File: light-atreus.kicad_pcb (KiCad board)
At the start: 2 copper layers, 37.4 x 44.1 mm, 8 parts, among them J1 USB_OTG, J2 CONN_01X02, J3 CONN_01X02, J4 USB_OTG, J5 CONN_01X02, J6 CONN_01X02

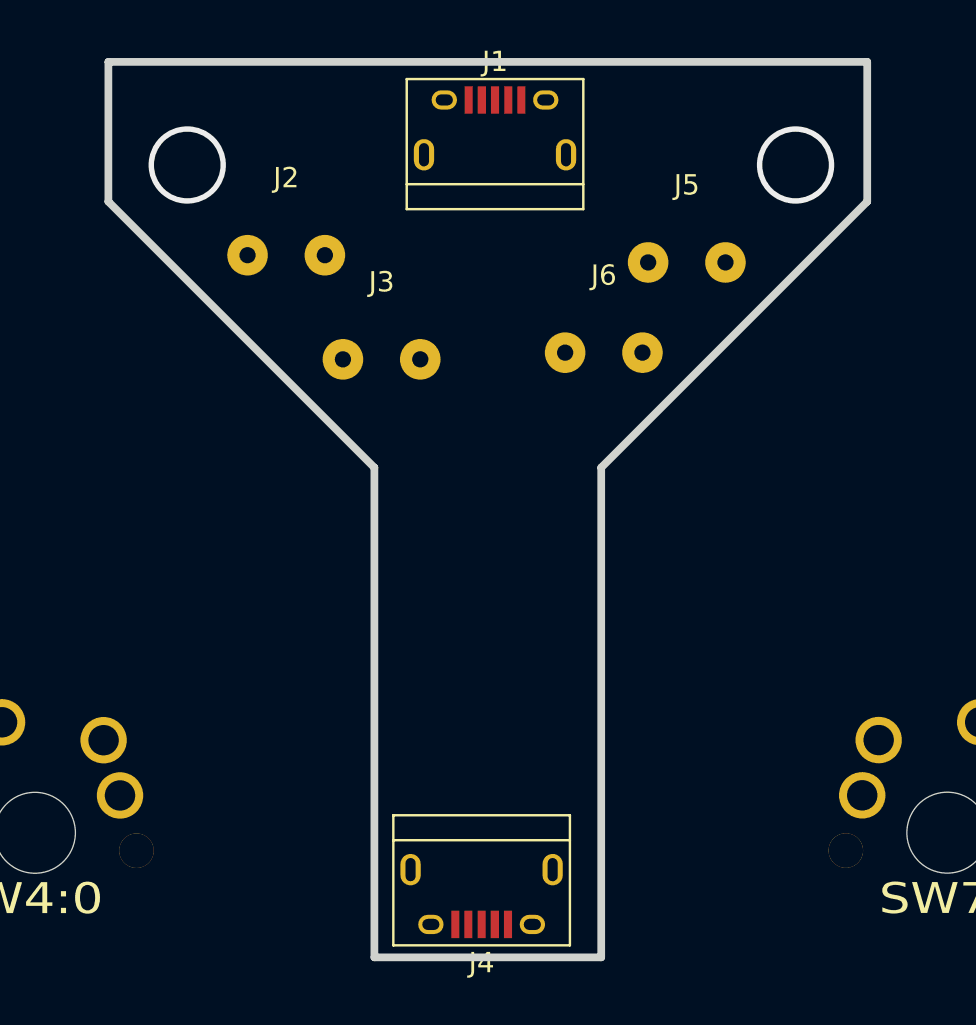
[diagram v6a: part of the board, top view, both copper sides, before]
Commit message: Add backside ground pour
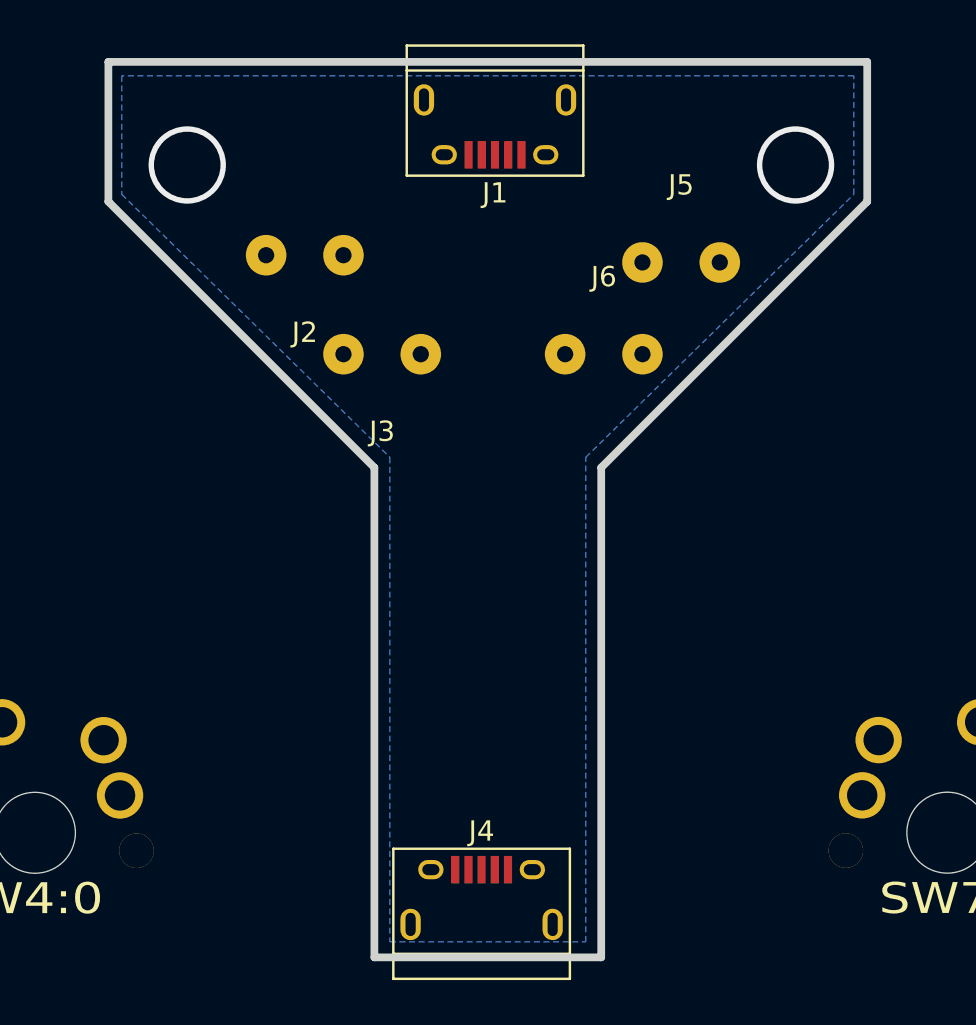
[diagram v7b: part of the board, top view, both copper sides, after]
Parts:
- moved J2 0.91 mm to (123.6, 99.3), turned to 180 degrees
- moved J5 0.28 mm to (142.1, 99.6)
- moved J3 0.26 mm to (127.4, 104.1), turned to 180 degrees
- moved J6 0.08 mm to (138.3, 104.1)
- turned J1 to 180 degrees
- turned J4 to 0 degrees
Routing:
- added copper zone on B.Cu, net /GND
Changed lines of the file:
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@@
   )
   (module Connectors:USB_Micro-B (layer Front)
-    (at 132.9436 92.964)
+    (at 132.9436 92.964 180)
     (descr "Micro USB Type B Receptacle")
     (tags "USB USB_B USB_micro USB_OTG")
     (attr smd)
-    (fp_text reference J1 (at 0 -3.24) (layer F.SilkS)
+    (fp_text reference J1 (at 0 -3.24 180) (layer F.SilkS)
       (effects (font (size 1 1) (thickness 0.15)))
     )
-    (fp_text value USB_OTG (at 0 5.01) (layer F.Fab)
+    (fp_text value USB_OTG (at 0 5.01 180) (layer F.Fab)
       (effects (font (size 1 1) (thickness 0.15)))
     )
@@
     (fp_line (start 4.6 -2.59) (end 4.6 4.26) (layer F.CrtYd) (width 0.05))
     (fp_line (start -4.6 -2.59) (end 4.6 -2.59) (layer F.CrtYd) (width 0.05))
-    (pad 6 thru_hole oval (at 3.5 1.35 90) (size 1.55 1) (drill oval 1.15 0.5) (layers *.Cu *.Mask)
+    (pad 6 thru_hole oval (at 3.5 1.35 270) (size 1.55 1) (drill oval 1.15 0.5) (layers *.Cu *.Mask)
       (net 5 "Net-(J1-Pad6)"))
-    (pad 6 thru_hole oval (at -3.5 1.35 90) (size 1.55 1) (drill oval 1.15 0.5) (layers *.Cu *.Mask)
+    (pad 6 thru_hole oval (at -3.5 1.35 270) (size 1.55 1) (drill oval 1.15 0.5) (layers *.Cu *.Mask)
       (net 5 "Net-(J1-Pad6)"))
-    (pad 6 thru_hole oval (at 2.5 -1.35 90) (size 0.95 1.25) (drill oval 0.55 0.85) (layers *.Cu *.Mask)
+    (pad 6 thru_hole oval (at 2.5 -1.35 270) (size 0.95 1.25) (drill oval 0.55 0.85) (layers *.Cu *.Mask)
       (net 5 "Net-(J1-Pad6)"))
-    (pad 6 thru_hole oval (at -2.5 -1.35 90) (size 0.95 1.25) (drill oval 0.55 0.85) (layers *.Cu *.Mask)
+    (pad 6 thru_hole oval (at -2.5 -1.35 270) (size 0.95 1.25) (drill oval 0.55 0.85) (layers *.Cu *.Mask)
       (net 5 "Net-(J1-Pad6)"))
-    (pad 5 smd rect (at 1.3 -1.35 90) (size 1.35 0.4) (layers Front F.Paste F.Mask)
+    (pad 5 smd rect (at 1.3 -1.35 270) (size 1.35 0.4) (layers Front F.Paste F.Mask)
       (net 9 /GND))
-    (pad 4 smd rect (at 0.65 -1.35 90) (size 1.35 0.4) (layers Front F.Paste F.Mask)
+    (pad 4 smd rect (at 0.65 -1.35 270) (size 1.35 0.4) (layers Front F.Paste F.Mask)
       (net 6 "Net-(J1-Pad4)"))
-    (pad 3 smd rect (at 0 -1.35 90) (size 1.35 0.4) (layers Front F.Paste F.Mask)
+    (pad 3 smd rect (at 0 -1.35 270) (size 1.35 0.4) (layers Front F.Paste F.Mask)
       (net 7 "Net-(J1-Pad3)"))
-    (pad 2 smd rect (at -0.65 -1.35 90) (size 1.35 0.4) (layers Front F.Paste F.Mask)
+    (pad 2 smd rect (at -0.65 -1.35 270) (size 1.35 0.4) (layers Front F.Paste F.Mask)
       (net 8 "Net-(J1-Pad2)"))
-    (pad 1 smd rect (at -1.3 -1.35 90) (size 1.35 0.4) (layers Front F.Paste F.Mask)
+    (pad 1 smd rect (at -1.3 -1.35 270) (size 1.35 0.4) (layers Front F.Paste F.Mask)
       (net 10 /VBUS))
   )
   (module Connectors:USB_Micro-B (layer Front)
-    (at 132.2832 130.8862 180)
+    (at 132.2832 130.8862)
     (descr "Micro USB Type B Receptacle")
     (tags "USB USB_B USB_micro USB_OTG")
     (attr smd)
-    (fp_text reference J4 (at 0 -3.24 180) (layer F.SilkS)
+    (fp_text reference J4 (at 0 -3.24) (layer F.SilkS)
       (effects (font (size 1 1) (thickness 0.15)))
     )
-    (fp_text value USB_OTG (at 0 5.01 180) (layer F.Fab)
+    (fp_text value USB_OTG (at 0 5.01) (layer F.Fab)
       (effects (font (size 1 1) (thickness 0.15)))
     )
@@
     (fp_line (start 4.35 2.8) (end -4.35 2.8) (layer F.SilkS) (width 0.12))
     (fp_line (start -4.35 4.03) (end -4.35 -2.38) (layer F.SilkS) (width 0.12))
-    (pad 1 smd rect (at -1.3 -1.35 270) (size 1.35 0.4) (layers Front F.Paste F.Mask)
+    (pad 1 smd rect (at -1.3 -1.35 90) (size 1.35 0.4) (layers Front F.Paste F.Mask)
       (net 10 /VBUS))
-    (pad 2 smd rect (at -0.65 -1.35 270) (size 1.35 0.4) (layers Front F.Paste F.Mask)
+    (pad 2 smd rect (at -0.65 -1.35 90) (size 1.35 0.4) (layers Front F.Paste F.Mask)
       (net 8 "Net-(J1-Pad2)"))
-    (pad 3 smd rect (at 0 -1.35 270) (size 1.35 0.4) (layers Front F.Paste F.Mask)
+    (pad 3 smd rect (at 0 -1.35 90) (size 1.35 0.4) (layers Front F.Paste F.Mask)
       (net 7 "Net-(J1-Pad3)"))
-    (pad 4 smd rect (at 0.65 -1.35 270) (size 1.35 0.4) (layers Front F.Paste F.Mask)
+    (pad 4 smd rect (at 0.65 -1.35 90) (size 1.35 0.4) (layers Front F.Paste F.Mask)
       (net 6 "Net-(J1-Pad4)"))
-    (pad 5 smd rect (at 1.3 -1.35 270) (size 1.35 0.4) (layers Front F.Paste F.Mask)
+    (pad 5 smd rect (at 1.3 -1.35 90) (size 1.35 0.4) (layers Front F.Paste F.Mask)
       (net 9 /GND))
-    (pad 6 thru_hole oval (at -2.5 -1.35 270) (size 0.95 1.25) (drill oval 0.55 0.85) (layers *.Cu *.Mask)
+    (pad 6 thru_hole oval (at -2.5 -1.35 90) (size 0.95 1.25) (drill oval 0.55 0.85) (layers *.Cu *.Mask)
       (net 5 "Net-(J1-Pad6)"))
-    (pad 6 thru_hole oval (at 2.5 -1.35 270) (size 0.95 1.25) (drill oval 0.55 0.85) (layers *.Cu *.Mask)
+    (pad 6 thru_hole oval (at 2.5 -1.35 90) (size 0.95 1.25) (drill oval 0.55 0.85) (layers *.Cu *.Mask)
       (net 5 "Net-(J1-Pad6)"))
-    (pad 6 thru_hole oval (at -3.5 1.35 270) (size 1.55 1) (drill oval 1.15 0.5) (layers *.Cu *.Mask)
+    (pad 6 thru_hole oval (at -3.5 1.35 90) (size 1.55 1) (drill oval 1.15 0.5) (layers *.Cu *.Mask)
       (net 5 "Net-(J1-Pad6)"))
-    (pad 6 thru_hole oval (at 3.5 1.35 270) (size 1.55 1) (drill oval 1.15 0.5) (layers *.Cu *.Mask)
+    (pad 6 thru_hole oval (at 3.5 1.35 90) (size 1.55 1) (drill oval 1.15 0.5) (layers *.Cu *.Mask)
       (net 5 "Net-(J1-Pad6)"))
   )
   (module custom_footprints:SolderWirePad_1x2-8mm (layer Front)
-    (at 122.6566 99.2632)
-    (fp_text reference J2 (at 0 -3.81) (layer F.SilkS)
+    (at 123.571 99.2632 180)
+    (fp_text reference J2 (at 0 -3.81 180) (layer F.SilkS)
       (effects (font (size 1 1) (thickness 0.15)))
     )
-    (fp_text value CONN_01X02 (at 0.635 2.54) (layer F.Fab)
+    (fp_text value CONN_01X02 (at 0.635 2.54 180) (layer F.Fab)
       (effects (font (size 1 1) (thickness 0.15)))
     )
-    (pad 2 thru_hole circle (at 1.905 0) (size 1.99898 1.99898) (drill 0.8001) (layers *.Cu *.Mask))
-    (pad 1 thru_hole circle (at -1.905 0) (size 1.99898 1.99898) (drill 0.8001) (layers *.Cu *.Mask)
+    (pad 2 thru_hole circle (at 1.905 0 180) (size 1.99898 1.99898) (drill 0.8001) (layers *.Cu *.Mask))
+    (pad 1 thru_hole circle (at -1.905 0 180) (size 1.99898 1.99898) (drill 0.8001) (layers *.Cu *.Mask)
       (net 10 /VBUS))
   )
   (module custom_footprints:SolderWirePad_1x2-8mm (layer Front)
-    (at 127.3556 104.394)
-    (fp_text reference J3 (at 0 -3.81) (layer F.SilkS)
+    (at 127.381 104.14 180)
+    (fp_text reference J3 (at 0 -3.81 180) (layer F.SilkS)
       (effects (font (size 1 1) (thickness 0.15)))
     )
-    (fp_text value CONN_01X02 (at 0.635 2.54) (layer F.Fab)
+    (fp_text value CONN_01X02 (at 0.635 2.54 180) (layer F.Fab)
       (effects (font (size 1 1) (thickness 0.15)))
     )
-    (pad 1 thru_hole circle (at -1.905 0) (size 1.99898 1.99898) (drill 0.8001) (layers *.Cu *.Mask)
+    (pad 1 thru_hole circle (at -1.905 0 180) (size 1.99898 1.99898) (drill 0.8001) (layers *.Cu *.Mask)
       (net 9 /GND))
-    (pad 2 thru_hole circle (at 1.905 0) (size 1.99898 1.99898) (drill 0.8001) (layers *.Cu *.Mask))
+    (pad 2 thru_hole circle (at 1.905 0 180) (size 1.99898 1.99898) (drill 0.8001) (layers *.Cu *.Mask))
   )
   (module custom_footprints:SolderWirePad_1x2-8mm (layer Front)
-    (at 142.3924 99.6188)
+    (at 142.113 99.6188)
     (fp_text reference J5 (at 0 -3.81) (layer F.SilkS)
       (effects (font (size 1 1) (thickness 0.15)))
@@
   )
   (module custom_footprints:SolderWirePad_1x2-8mm (layer Front)
-    (at 138.303 104.0638)
+    (at 138.303 104.14)
     (fp_text reference J6 (at 0 -3.81) (layer F.SilkS)
       (effects (font (size 1 1) (thickness 0.15)))
@@
   (via (at 117.7798 94.8182) (size 3.81) (drill 3.2766) (layers Front Back) (net 0))
   (via (at 147.7518 94.8182) (size 3.81) (drill 3.2766) (layers Front Back) (net 0))
+  (zone (net 9) (net_name /GND) (layer Back) (hatch edge 0.508)
+    (connect_pads (clearance 0.508))
+    (min_thickness 0.254)
+    (fill yes (arc_segments 16) (thermal_gap 0.508) (thermal_bridge_width 0.508))
+    (polygon
+      (pts
+        (xy 114.554 90.424) (xy 114.554 96.266) (xy 127.762 109.22) (xy 127.762 133.096) (xy 137.414 133.096)
+        (xy 137.414 109.22) (xy 150.622 96.266) (xy 150.622 90.424)
+      )
+    )
+  )
 )

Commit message: Re-place changed wire-pad footprints
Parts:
- moved J2 2.17 mm to (121.4, 99.1)
- moved J3 1.71 mm to (126.2, 102.9)
- moved J6 1.71 mm to (139.4, 102.9)
- moved J5 1.50 mm to (143.5, 99.1)
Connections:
- J2 pad 2: (no net) -> Net-(J2-Pad2)
- J3 pad 2: (no net) -> Net-(J3-Pad2)
- J5 pad 2: (no net) -> Net-(J5-Pad2)
- J6 pad 2: (no net) -> Net-(J6-Pad2)
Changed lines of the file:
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@@
     (zones 0)
     (modules 8)
-    (nets 11)
+    (nets 15)
   )
   (page A4)
@@
   (net 9 /GND)
   (net 10 /VBUS)
+  (net 11 "Net-(J2-Pad2)")
+  (net 12 "Net-(J3-Pad2)")
+  (net 13 "Net-(J5-Pad2)")
+  (net 14 "Net-(J6-Pad2)")
   (net_class Default "This is the default net class."
     (clearance 0)
@@
     (add_net "Net-(J1-Pad4)")
     (add_net "Net-(J1-Pad6)")
+    (add_net "Net-(J2-Pad2)")
+    (add_net "Net-(J3-Pad2)")
+    (add_net "Net-(J5-Pad2)")
+    (add_net "Net-(J6-Pad2)")
   )
   (module MX_FLIP locked (layer Front)
@@
   )
   (module custom_footprints:SolderWirePad_1x2-8mm (layer Front)
-    (at 123.571 99.2632 180)
+    (at 121.412 99.06 180)
     (fp_text reference J2 (at 0 -3.81 180) (layer F.SilkS)
       (effects (font (size 1 1) (thickness 0.15)))
@@
       (effects (font (size 1 1) (thickness 0.15)))
     )
-    (pad 2 thru_hole circle (at 1.905 0 180) (size 1.99898 1.99898) (drill 0.8001) (layers *.Cu *.Mask))
-    (pad 1 thru_hole circle (at -1.905 0 180) (size 1.99898 1.99898) (drill 0.8001) (layers *.Cu *.Mask)
-      (net 10 /VBUS))
-  )
-  (module custom_footprints:SolderWirePad_1x2-8mm (layer Front)
-    (at 127.381 104.14 180)
+    (pad 2 thru_hole circle (at 1.1 0 180) (size 1.99898 1.99898) (drill 0.8001) (layers *.Cu *.Mask)
+      (net 11 "Net-(J2-Pad2)"))
+    (pad 1 thru_hole circle (at -1.11 0 180) (size 1.99898 1.99898) (drill 0.8001) (layers *.Cu *.Mask)
+      (net 10 /VBUS))
+  )
+  (module custom_footprints:SolderWirePad_1x2-8mm (layer Front)
+    (at 126.238 102.87 180)
     (fp_text reference J3 (at 0 -3.81 180) (layer F.SilkS)
       (effects (font (size 1 1) (thickness 0.15)))
@@
       (effects (font (size 1 1) (thickness 0.15)))
     )
-    (pad 1 thru_hole circle (at -1.905 0 180) (size 1.99898 1.99898) (drill 0.8001) (layers *.Cu *.Mask)
-      (net 9 /GND))
-    (pad 2 thru_hole circle (at 1.905 0 180) (size 1.99898 1.99898) (drill 0.8001) (layers *.Cu *.Mask))
-  )
-  (module custom_footprints:SolderWirePad_1x2-8mm (layer Front)
-    (at 142.113 99.6188)
+    (pad 1 thru_hole circle (at -1.11 0 180) (size 1.99898 1.99898) (drill 0.8001) (layers *.Cu *.Mask)
+      (net 9 /GND))
+    (pad 2 thru_hole circle (at 1.1 0 180) (size 1.99898 1.99898) (drill 0.8001) (layers *.Cu *.Mask)
+      (net 12 "Net-(J3-Pad2)"))
+  )
+  (module custom_footprints:SolderWirePad_1x2-8mm (layer Front)
+    (at 143.51 99.06)
     (fp_text reference J5 (at 0 -3.81) (layer F.SilkS)
       (effects (font (size 1 1) (thickness 0.15)))
@@
       (effects (font (size 1 1) (thickness 0.15)))
     )
-    (pad 2 thru_hole circle (at 1.905 0) (size 1.99898 1.99898) (drill 0.8001) (layers *.Cu *.Mask))
-    (pad 1 thru_hole circle (at -1.905 0) (size 1.99898 1.99898) (drill 0.8001) (layers *.Cu *.Mask)
-      (net 10 /VBUS))
-  )
-  (module custom_footprints:SolderWirePad_1x2-8mm (layer Front)
-    (at 138.303 104.14)
+    (pad 2 thru_hole circle (at 1.1 0) (size 1.99898 1.99898) (drill 0.8001) (layers *.Cu *.Mask)
+      (net 13 "Net-(J5-Pad2)"))
+    (pad 1 thru_hole circle (at -1.11 0) (size 1.99898 1.99898) (drill 0.8001) (layers *.Cu *.Mask)
+      (net 10 /VBUS))
+  )
+  (module custom_footprints:SolderWirePad_1x2-8mm (layer Front)
+    (at 139.446 102.87)
     (fp_text reference J6 (at 0 -3.81) (layer F.SilkS)
       (effects (font (size 1 1) (thickness 0.15)))
@@
       (effects (font (size 1 1) (thickness 0.15)))
     )
-    (pad 1 thru_hole circle (at -1.905 0) (size 1.99898 1.99898) (drill 0.8001) (layers *.Cu *.Mask)
-      (net 9 /GND))
-    (pad 2 thru_hole circle (at 1.905 0) (size 1.99898 1.99898) (drill 0.8001) (layers *.Cu *.Mask))
+    (pad 1 thru_hole circle (at -1.11 0) (size 1.99898 1.99898) (drill 0.8001) (layers *.Cu *.Mask)
+      (net 9 /GND))
+    (pad 2 thru_hole circle (at 1.1 0) (size 1.99898 1.99898) (drill 0.8001) (layers *.Cu *.Mask)
+      (net 14 "Net-(J6-Pad2)"))
   )
   (gr_line (start 151.2824 96.6216) (end 138.176 109.728) (layer Edge.Cuts) (width 0.381))
